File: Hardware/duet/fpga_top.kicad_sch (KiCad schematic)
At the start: 7 parts, among them U1 LFE5U-45F-6BG256C

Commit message: Add ECP5 configuration pins and labels
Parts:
- added R1: 10k, symbol Device:R
- added X1: OT322525MJBA4SL, easyeda2kicad:OSC-SMD_4P-L3.2-W2.5-BL, symbol easyeda2kicad:OT322525MJBA4SL
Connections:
- net GND: now also X1.2 (GND)
- net FPGA-PCLK: now reaches U1.B8 (PT44B/PCLKC1_0)
- net FPGA-PCLK: now also X1.3 (OUT)
- net +3.3V: now reaches U1.L6 (VCCIO8)
- net +3.3V: now also R1.1, X1.4 (VDD)
- net FPGA-TDO: now reaches U1.M10 (TDO)
- net FLASH-IO2: now reaches U1.M7 (PB9B/D2/IO2)
- net FLASH-IO3: now reaches U1.N7 (PB9A/D3/IO3)
- net FLASH-~{CS}: now reaches U1.N8 (PB15A/HOLDN/DI/BUSY/CSSPIN/CEN)
- net FLASH-CLK: now reaches U1.N9 (CCLK/MCLK/SCK)
- net FPGA-DONE: now reaches U1.P9 (DONE)
- net FPGA-TDI: now reaches U1.R11 (TDI)
- net FPGA-PROGRAMN: now reaches U1.R9 (PROGRAMN)
- net FPGA-TCK: now reaches U1.T10 (TCK)
- net FPGA-TMS: now reaches U1.T11 (TMS)
- net FLASH-IO1: now reaches U1.T7 (PB11A/D1/MISO/IO1)
- net FLASH-IO0: now reaches U1.T8 (PB11B/D0/MOSI/IO0)
- net FPGA-INITN: now reaches U1.T9 (INITN)
- net RAM-D0 renamed RAM-DQ0
- net RAM-D1 renamed RAM-DQ1
- net RAM-D2 renamed RAM-DQ2
- net RAM-D3 renamed RAM-DQ3
- net RAM-D4 renamed RAM-DQ4
- net RAM-D5 renamed RAM-DQ5
- net RAM-D6 renamed RAM-DQ6
- net RAM-D7 renamed RAM-DQ7
- new net: R1.2, X1.1 (Enable/Disable)
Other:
- note added: "25 MHz oscillator"
- note added: "Bank 0"
- note added: "Bank 1"
- note added: "Bank 3"
- note added: "Bank 6"
- note added: "Bank 7"
- note added: "TODO: Add JTAG header"
- note added: "TODO: Add pull-down / up resistors for 4.7k pull ups - CFG, INITN, PROGRAMN, FLASH-~{CS} and WRITEN 500R pull down - CFG_0 and CFG_2"
- note added: "TODO: CSxN pulled up through 4.7k"
- note added: "TODO: Status LEDs on IO[4..7]"
- note added: "TODO: Wire up Vcc AUX to 2.5 V with debounce capacitors"
- note added: "TODO: debouncing caps 100 nF 10 nF"
- moved on the sheet: U1A, U1B

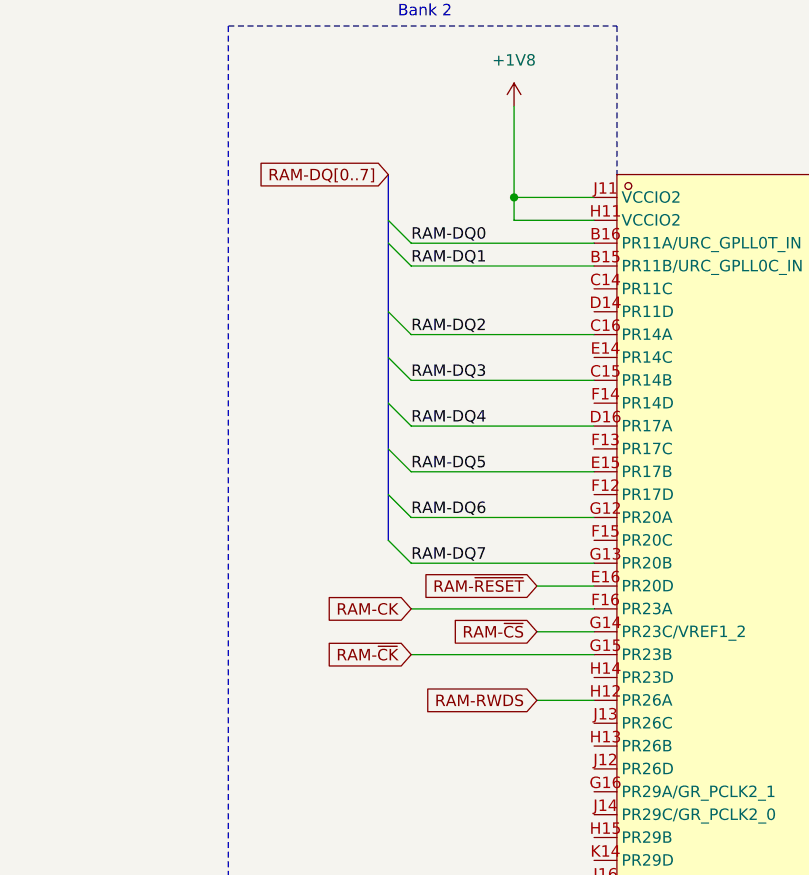
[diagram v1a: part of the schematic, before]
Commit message: Adds HDMI transmitter and connector
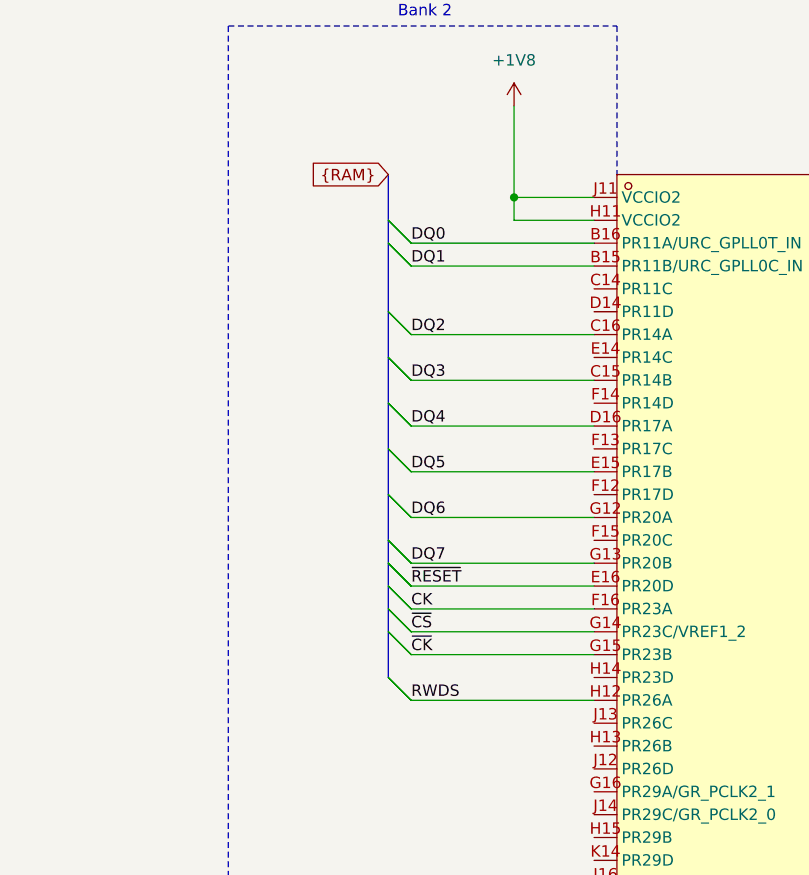
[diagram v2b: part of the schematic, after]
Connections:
- net RAM-CK renamed CK
- net RAM-DQ0 renamed DQ0
- net RAM-DQ1 renamed DQ1
- net RAM-DQ2 renamed DQ2
- net RAM-DQ3 renamed DQ3
- net RAM-DQ4 renamed DQ4
- net RAM-DQ5 renamed DQ5
- net RAM-DQ6 renamed DQ6
- net RAM-DQ7 renamed DQ7
- net RAM-RWDS renamed RWDS
- net RAM-~{CK} renamed ~{CK}
- net RAM-~{CS} renamed ~{CS}
- net RAM-~{RESET} renamed ~{RESET}

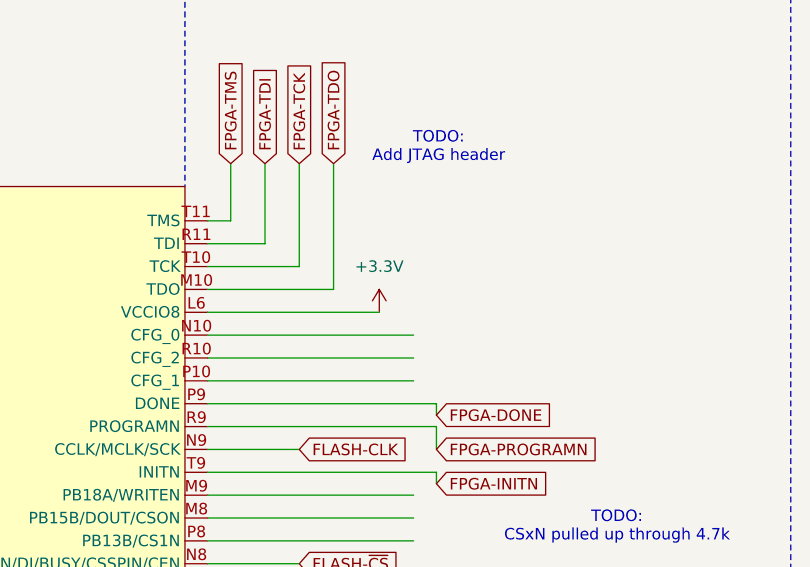
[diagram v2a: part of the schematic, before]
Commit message: Adds ESP32 and pull up-down resistors
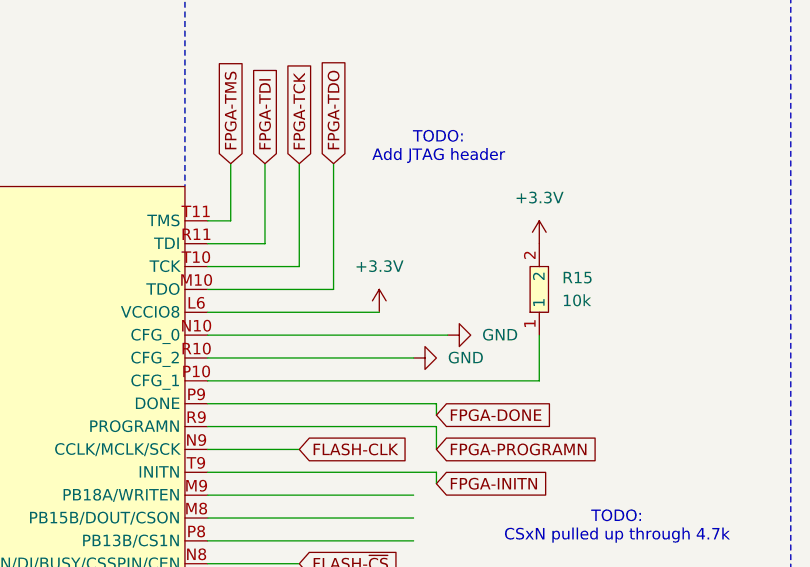
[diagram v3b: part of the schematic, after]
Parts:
- added R15: 10k, easyeda2kicad:R0402, symbol easyeda2kicad:0402WGF1002TCE
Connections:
- net +3.3V: now also R15.2
- net GND: now also U1.N10 (CFG_0), U1.R10 (CFG_2)
- net at U1.P10 (CFG_1): now also R15.1

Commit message: Add mezzanine connector and finalze HDMI
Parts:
- removed R15: 10k, easyeda2kicad:R0402, symbol easyeda2kicad:0402WGF1002TCE
- added R15, R32: 470R, easyeda2kicad:R0402, symbol easyeda2kicad:0402WGF4700TCE
- added R21, R28, R29, R30, R31: 4.7k, easyeda2kicad:R0402, symbol easyeda2kicad:0402WGF4701TCE
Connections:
- net +3.3V: now also R28.2, R29.2, R30.2, R31.2
- net FPGA-PCLK: now also U1.A8 (PT38B/PCLKC0_0); no longer U1.B8 (PT44B/PCLKC1_0)
- net GND: now also R15.2, R21.2, R32.2; no longer U1.N10 (CFG_0), U1.R10 (CFG_2)
- net D9: now reaches U1.A10 (PT51B)
- net D16: now reaches U1.A11 (PT71A)
- net D18: now reaches U1.A12 (PT71B)
- net CI2CA: now reaches U1.A15 (PT85B/URC_GPLL1C_IN)
- net CI2CA: now also R21.1
- net SD0: now reaches U1.A2 (PT4A/ULC_GPLL1T_IN)
- net SD1: now reaches U1.A3 (PT6A)
- net SD3: now reaches U1.A4 (PT6B)
- net D7: now reaches U1.A9 (PT51A)
- net D8: now reaches U1.B10 (PT53A)
- net D12: now reaches U1.B11 (PT58A)
- net D19: now reaches U1.B12 (PT74A)
- net D23: now reaches U1.B13 (PT78A)
- net SD2: now reaches U1.B3 (PT4B/ULC_GPLL1C_IN)
- net SPDIF: now reaches U1.B4 (PT11B)
- net D3: now reaches U1.B9 (PT47A/GR_PCLK1_0)
- net D10: now reaches U1.C10 (PT53B)
- net D14: now reaches U1.C11 (PT58B)
- net D21: now reaches U1.C12 (PT74B)
- net HSYNC: now reaches U1.C13 (PT78B)
- net SCK: now reaches U1.C4 (PT11A)
- net D0: now reaches U1.C8 (PT44A/PCLKT1_0)
- net D5: now reaches U1.C9 (PT47B/GR_PCLK1_1)
- net D11: now reaches U1.D10 (PT56A)
- net D15: now reaches U1.D11 (PT69A)
- net D20: now reaches U1.D12 (PT76A)
- net DE: now reaches U1.D13 (PT80A)
- net WS: now reaches U1.D4 (PT9B)
- net D1: now reaches U1.D8 (PT42B/PCLKC1_1)
- net D4: now reaches U1.D9 (PT49A)
- net D13: now reaches U1.E10 (PT56B)
- net D17: now reaches U1.E11 (PT69B)
- net D22: now reaches U1.E12 (PT76B)
- net VSYNC: now reaches U1.E13 (PT80B)
- net MCLK: now reaches U1.E4 (PT9A)
- net IDCK: now reaches U1.E8 (PT42A/PCLKT1_1)
- net D6: now reaches U1.E9 (PT49B)
- net CFG_2: now reaches U1.P10 (CFG_1)
- net CFG_2: now also R32.1
- net FPGA-CS0N: now reaches U1.M8 (PB15B/DOUT/CSON)
- net FPGA-CS0N: now also R29.1
- net FPGA-WRITEN: now reaches U1.M9 (PB18A/WRITEN)
- net FPGA-WRITEN: now also R28.1
- net FPGA-CS1N: now reaches U1.P8 (PB13B/CS1N)
- net FPGA-CS1N: now also R30.1
- new net CFG_0: R15.1, U1.N10 (CFG_0)
- new net CFG_1: R31.1, U1.R10 (CFG_2)
- new net D2: U1.B8 (PT44B/PCLKC1_0)
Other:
- note added: "TODO: Add 3.3V"
- note removed: "TODO: CSxN pulled up through 4.7k"
- moved on the sheet: R1, U1C, X1
